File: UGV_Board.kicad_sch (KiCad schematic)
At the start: 19 parts, among them J1 I2C_EXPANSION, J2 Debug Header, J3 ESP_Header, SW1 SW_MCU_EN, SW2 SW_PICO_RST, SW3 SW_ESP_RST, U1 SC0915, U2 SPX1117M3-L-3-3

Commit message: mcu control circuitry
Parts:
- added C?: 1uF, symbol Device:C
- added J?: RFLCTL_Header, symbol Connector:Conn_01x04_Female
- added J?: RFLCTR_Header, symbol Connector:Conn_01x04_Female
- added R? (x4): 330, Resistor_SMD:R_1206_3216Metric_Pad1.30x1.75mm_HandSolder, symbol Device:R_Small_US
- added R? (x2): 10k, Resistor_SMD:R_1206_3216Metric_Pad1.30x1.75mm_HandSolder, symbol Device:R_Small_US
- added RV? (x2): R_Potentiometer, symbol Device:R_Potentiometer
- added U? (x3): LM393, symbol Comparator:LM393
- J1: symbol Connector:Conn_01x02_Female -> Connector:Conn_01x04_Female
- R1, R2, R3, R4, R5, R6: value 220 -> 330
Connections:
- net +3V3: now also J1.4 (Pin_4), J?.2 (Pin_2), J?.2 (Pin_2), J?.4 (Pin_4), J?.4 (Pin_4), R?.2, R?.2, RV?.1, RV?.1, U?.8 (V+)
- net GND: now also J1.1 (Pin_1), C?.2, R?.1, R?.1, R?.1, R?.1, RV?.3, RV?.3, U?.4 (V-)
- net SCL: now also J1.2 (Pin_2), R?.1; no longer J1.1 (Pin_1)
- net SDA: now also J1.3 (Pin_3), R?.1; no longer J1.2 (Pin_2)
- net at SW2.1, U1.30 (RUN): now also C?.1
- net ENCL_SIG: now reaches U1.19 (I2C1_SDA/SPI1_SCK/GP14)
- net ENCL_SIG: now also U?.7
- net ENCR_SIG: now reaches U1.20 (I2C1_SCL/SPI1_TX/GP15)
- net ENCR_SIG: now also U?.1
- new net: J?.3 (Pin_3), R?.2 (x2)
- new net: RV?.2, U?.6 (_)
- new net: RV?.2, U?.2 (-)
- new net: J?.1 (Pin_1), R?.2, U?.3 (+)
- new net: J?.1 (Pin_1), R?.2, U?.5 (+)
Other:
- note added: "*ESP-01 reset switch, 12k pullup & 1uF debounce internal"
- note added: "*Igor/Yusuf feel free to make a separate ground line if you're going for total isolation. Delete this text when you're done. Also feel free to wipe this regulator with your own 3.3V line"
- note added: "*MCU PWR/IO line voltage, regulated: 3.3V max current: 800mA"
- note added: "*PICO reset swtich, 50k pullup internal"
- note added: "12k internal pullup"
- note added: "1k -> Blue LED, active low"
- note added: "Reflective Sensor + Comparator Logic"
- note removed: "*ESP-01 reset switch"
- note removed: "*Igor/Yusuf feel free to make a separate ground line if you're going for total isolation. Delete this text when you're done."
- note removed: "*MCU PWR/IO line"
- note removed: "*PICO reset swtich"
- moved on the sheet: D1, D3, R1, R3, R5

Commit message: Buck + H-Bridge
Added
-Buck Convertor
-H-Bridge
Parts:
- added C1: 10uF, symbol Device:C_Small
- added C2: 22uF, symbol Device:C_Small
- added C2: 22 uF, symbol Device:C_Small
- added C3: 100nF, symbol Device:C_Small
- added J7, J8: Conn_01x02_Female, symbol Connector:Conn_01x02_Female
- added L1: 4.7uH, symbol Device:L
- added R2: 10k, Resistor_SMD:R_1206_3216Metric_Pad1.30x1.75mm_HandSolder, symbol Device:R_Small_US
- added RV3: R_Potentiometer, symbol Device:R_Potentiometer
- added U4: BD63565EFV-E2, BD63565EFV-E2_ROM, symbol H bridge:BD63565EFV-E2
- added U5: AP62200WU-7, TSOT26-WU_DIO, symbol Buck Convertor:AP62200WU-7
- R10, R7, R8, R9: renamed from R?; value 330 -> 220
- gave numbers to parts that had none: 9
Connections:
- net +3V3: now also U4.17 (PS), U4.20 (VCC), U5.5 (EN)
- net +7.5V: now also C1.1, U5.3 (VIN)
- net GND: now also C1.2, C2.2, C2.2, R2.1, U4.1 (GND), U4.13 (PGND), U4.4 (PWM), U4.8 (PGND), U5.1 (GND)
- new net: C3.1, L1.2, U5.2 (SW)
- new net: R2.2, RV3.2, U5.4 (FB)
- new net: C3.2, U5.6 (BST)
- new net: J7.1 (Pin_1), U4.6 (OUT1A), U4.7 (OUT1A)
- new net: J7.2 (Pin_2), U4.10 (OUT1B), U4.9 (OUT1B)
- new net: J8.2 (Pin_2), U4.11 (OUT2B), U4.12 (OUT2B)
- new net: J8.1 (Pin_1), U4.14 (OUT2A), U4.15 (OUT2A)
- new net +6V: C2.1, C2.1, L1.1, RV3.3, U4.16 (VM), U4.5 (VM)
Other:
- note added: "Buck Convertor"
- note added: "H-Bridge"
- note added: "Pico-Microcontroller"
- moved on the sheet: J3

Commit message: Assigned footprints
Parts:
- C1, C2, C3, C4: footprint (none) -> Capacitor_SMD:C_1206_3216Metric_Pad1.33x1.80mm_HandSolder
- C5: renamed from C2; footprint (none) -> Capacitor_SMD:C_1206_3216Metric_Pad1.33x1.80mm_HandSolder
- J4, J5: footprint (none) -> Connector_PinSocket_2.54mm:PinSocket_1x04_P2.54mm_Vertical
- J6: footprint (none) -> Connector_PinSocket_2.54mm:PinSocket_1x08_P2.54mm_Vertical
- J7, J8: footprint (none) -> Connector_PinSocket_2.54mm:PinSocket_1x02_P2.54mm_Vertical
- L1: footprint (none) -> Inductor_SMD:L_1210_3225Metric_Pad1.42x2.65mm_HandSolder
- RV1, RV2, RV3: footprint (none) -> Potentiometer_SMD:Potentiometer_Bourns_TC33X_Vertical
- U3: footprint (none) -> Package_DIP:DIP-8_W7.62mm_LongPads
- U4: footprint BD63565EFV-E2_ROM -> Drivers_3rdParty:BD63565EFV-E2
- U5: footprint TSOT26-WU_DIO -> SMPS_3rdParty:AP62200WU-7
- renumbered R2 to R13
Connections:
- net +3V3 renamed +3.3V

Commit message: floating en pin
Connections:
- net +3.3V: no longer U5.5 (EN)
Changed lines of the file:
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@@
     (pin "3")
-  )
-  (symbol (lib_name "+3.3V_10") (lib_id "power:+3.3V") (at 398.78 124.46 270) (unit 1)
-    (in_bom yes) (on_board yes) (fields_autoplaced)
-    (property "Reference" "#PWR0134" (id 0) (at 394.97 124.46 0)
-      (effects (font (size 1.27 1.27)) hide)
-    )
-    (property "Value" "+3.3V" (id 1) (at 402.59 124.4599 90)
-      (effects (font (size 1.27 1.27)) (justify left))
-    )
-    (property "Footprint" "" (id 2) (at 398.78 124.46 0)
-      (effects (font (size 1.27 1.27)) hide)
-    )
-    (property "Datasheet" "" (id 3) (at 398.78 124.46 0)
-      (effects (font (size 1.27 1.27)) hide)
-    )
-    (pin "1")
   )
   (symbol (lib_id "Device:R_Potentiometer") (at 341.63 137.16 270) (unit 1)
@@
       (reference "#PWR0133") (unit 1) (value "GND") (footprint "")
     )
-    (path "/76fdc603-9607-4e8b-ba75-955278b1b684"
-      (reference "#PWR0134") (unit 1) (value "+3.3V") (footprint "")
-    )
     (path "/8a73a5c8-b6b2-4b9f-a45b-d6aa4f2ccad5"

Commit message: fixed i2c header footprint
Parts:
- J1: footprint Connector_PinSocket_2.54mm:PinSocket_1x02_P2.54mm_Vertical -> Connector_PinSocket_2.54mm:PinSocket_1x04_P2.54mm_Vertical
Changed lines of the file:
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@@
     (property "Reference" "J1" (id 0) (at 276.86 267.97 0))
     (property "Value" "I2C_EXPANSION" (id 1) (at 276.86 270.51 0))
-    (property "Footprint" "Connector_PinSocket_2.54mm:PinSocket_1x02_P2.54mm_Vertical" (id 2) (at 279.4 278.13 0)
+    (property "Footprint" "Connector_PinSocket_2.54mm:PinSocket_1x04_P2.54mm_Vertical" (id 2) (at 279.4 278.13 0)
       (effects (font (size 1.27 1.27)) hide)
     )
@@
     )
     (path "/42fa0348-d6f3-440b-802f-dcef76e8d02c"
-      (reference "J1") (unit 1) (value "I2C_EXPANSION") (footprint "Connector_PinSocket_2.54mm:PinSocket_1x02_P2.54mm_Vertical")
+      (reference "J1") (unit 1) (value "I2C_EXPANSION") (footprint "Connector_PinSocket_2.54mm:PinSocket_1x04_P2.54mm_Vertical")
     )
     (path "/75c2a44c-2138-4e6a-93e2-ed701bb8f3d2"

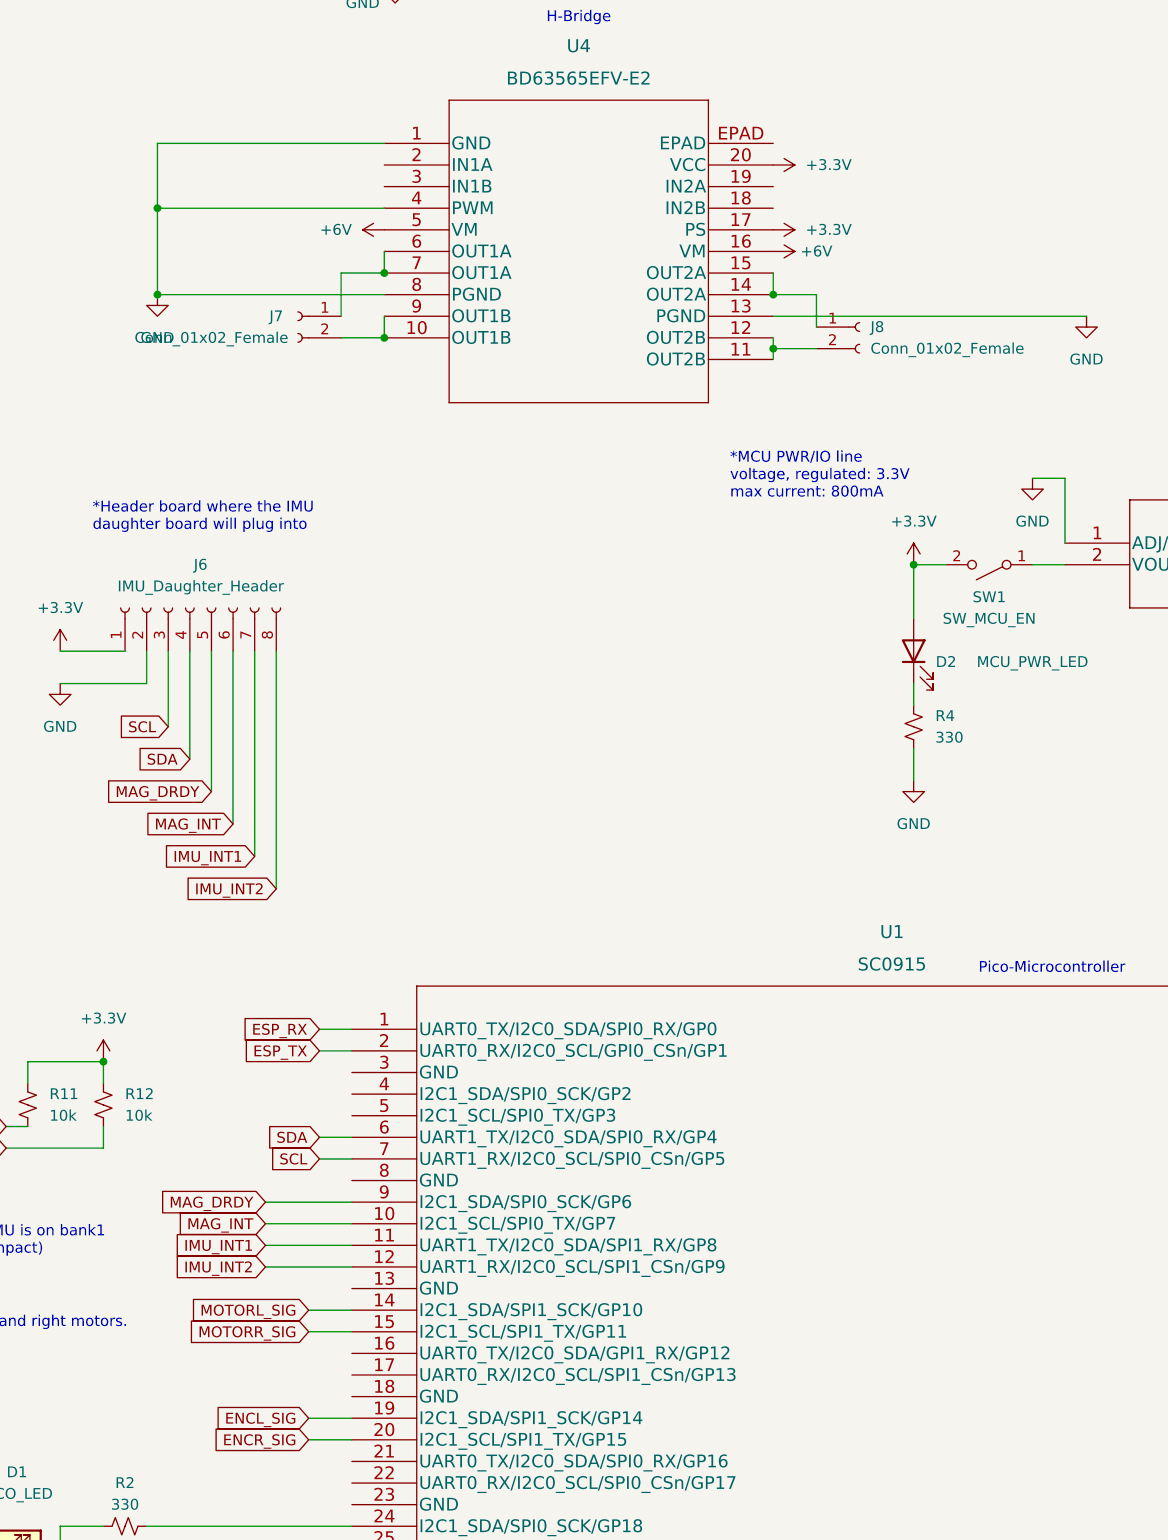
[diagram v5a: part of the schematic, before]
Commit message: plugged mcu into h-bridge
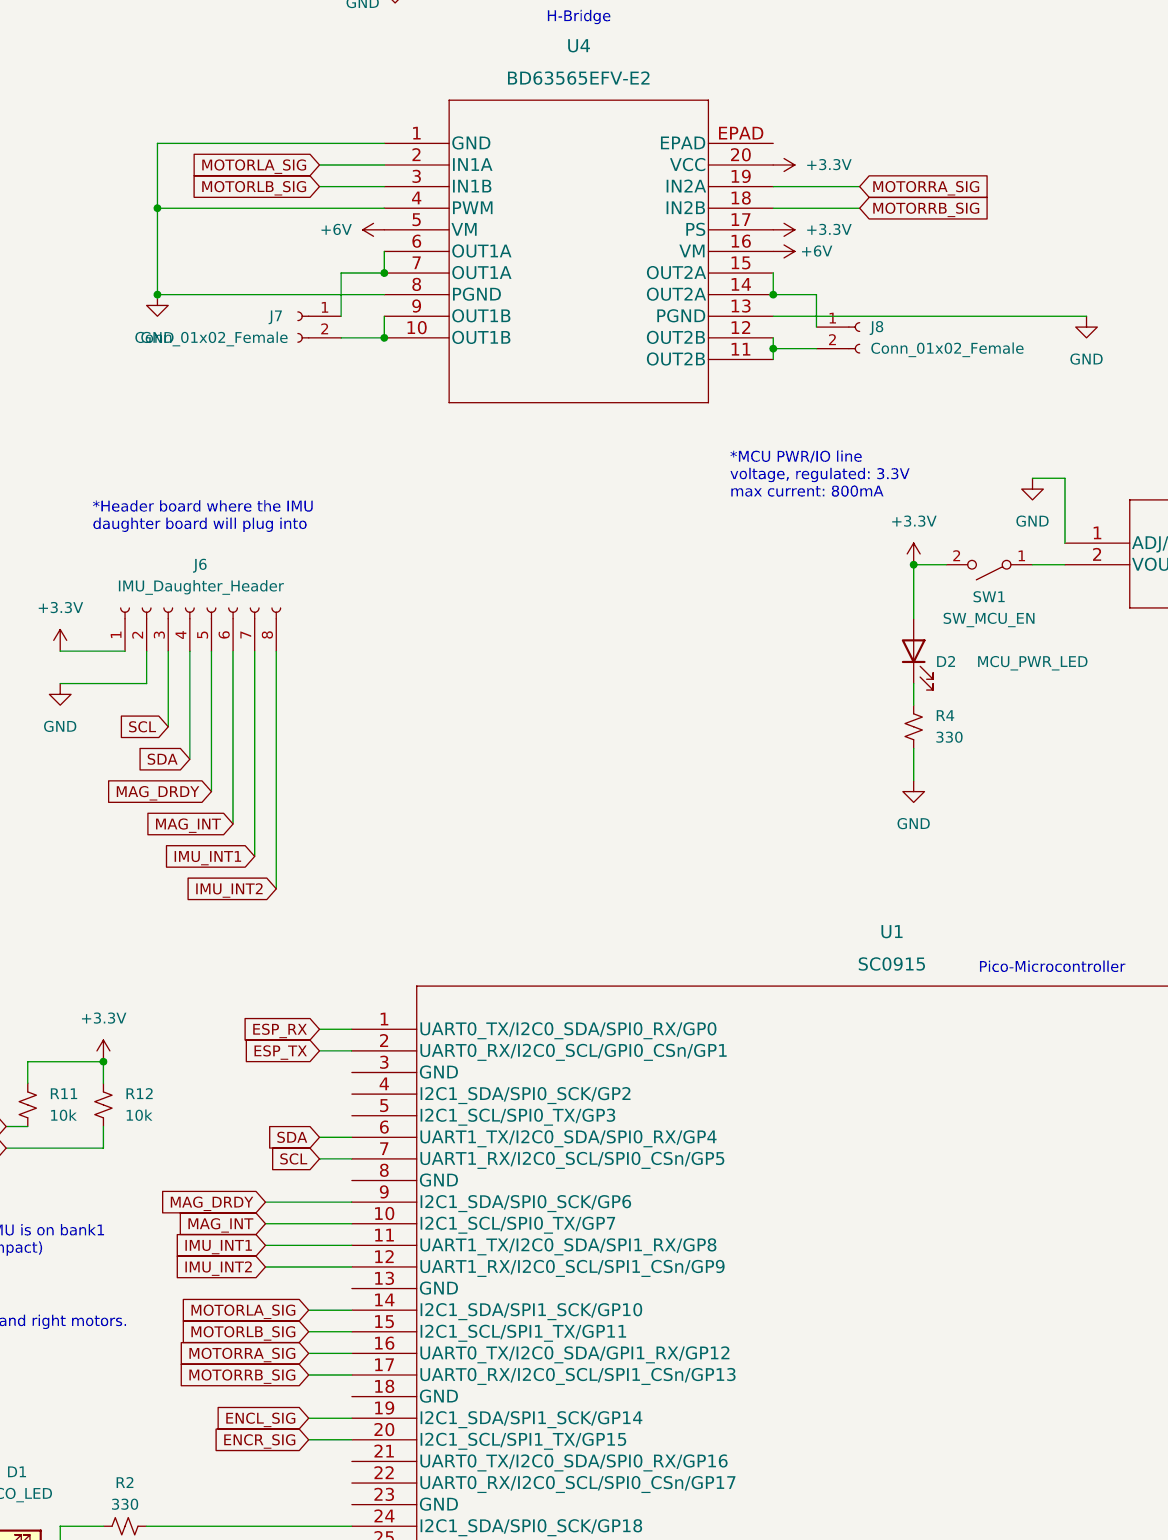
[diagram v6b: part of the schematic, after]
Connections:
- net MOTORL_SIG is gone; now on net MOTORLA_SIG: U1.14 (I2C1_SDA/SPI1_SCK/GP10)
- net MOTORR_SIG is gone; now on net MOTORLB_SIG: U1.15 (I2C1_SCL/SPI1_TX/GP11)
- net MOTORRB_SIG: now reaches U4.18 (IN2B)
- net MOTORRB_SIG: now also U1.17 (UART0_RX/I2C0_SCL/SPI1_CSn/GP13)
- net MOTORRA_SIG: now reaches U4.19 (IN2A)
- net MOTORRA_SIG: now also U1.16 (UART0_TX/I2C0_SDA/GPI1_RX/GP12)
- net MOTORLA_SIG: now reaches U4.2 (IN1A)
- net MOTORLB_SIG: now reaches U4.3 (IN1B)
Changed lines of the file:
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@@
+    (stroke (width 0) (type default) (color 0 0 0 0))
+  )
+  (wire (pts (xy 402.59 181.61) (xy 412.75 181.61))
     (stroke (width 0) (type default) (color 0 0 0 0))
   )
@@
     (stroke (width 0) (type default) (color 0 0 0 0))
   )
+  (wire (pts (xy 349.25 181.61) (xy 356.87 181.61))
+    (stroke (width 0) (type default) (color 0 0 0 0))
+  )
   (wire (pts (xy 177.8 365.76) (xy 223.52 365.76))
     (stroke (width 0) (type default) (color 0 0 0 0))
@@
     (stroke (width 0) (type default) (color 0 0 0 0))
   )
+  (wire (pts (xy 347.98 318.77) (xy 353.06 318.77))
+    (stroke (width 0) (type default) (color 0 0 0 0))
+  )
   (wire (pts (xy 284.48 278.13) (xy 289.56 278.13))
     (stroke (width 0) (type default) (color 0 0 0 0))
@@
     (stroke (width 0) (type default) (color 0 0 0 0))
   )
+  (wire (pts (xy 402.59 184.15) (xy 412.75 184.15))
+    (stroke (width 0) (type default) (color 0 0 0 0))
+  )
   (wire (pts (xy 224.79 287.02) (xy 224.79 289.56))
     (stroke (width 0) (type default) (color 0 0 0 0))
@@
     (stroke (width 0) (type default) (color 0 0 0 0))
   )
+  (wire (pts (xy 349.25 179.07) (xy 356.87 179.07))
+    (stroke (width 0) (type default) (color 0 0 0 0))
+  )
   (wire (pts (xy 557.53 259.08) (xy 560.07 259.08))
     (stroke (width 0) (type default) (color 0 0 0 0))
@@
   )
   (wire (pts (xy 187.96 360.68) (xy 187.96 367.03))
+    (stroke (width 0) (type default) (color 0 0 0 0))
+  )
+  (wire (pts (xy 347.98 321.31) (xy 353.06 321.31))
     (stroke (width 0) (type default) (color 0 0 0 0))
   )
@@
     )
   )
-  (global_label "MOTORR_SIG" (shape input) (at 347.98 316.23 180) (fields_autoplaced)
-    (effects (font (size 1.27 1.27)) (justify right))
-    (property "Intersheet References" "${INTERSHEET_REFS}" (id 0) (at 333.895 316.1506 0)
+  (global_label "MOTORLB_SIG" (shape input) (at 347.98 316.23 180) (fields_autoplaced)
+    (effects (font (size 1.27 1.27)) (justify right))
+    (property "Intersheet References" "${INTERSHEET_REFS}" (id 0) (at 332.8669 316.1506 0)
       (effects (font (size 1.27 1.27)) (justify right) hide)
     )
@@
     )
   )
+  (global_label "MOTORLA_SIG" (shape input) (at 349.25 179.07 180) (fields_autoplaced)
+    (effects (font (size 1.27 1.27)) (justify right))
+    (property "Intersheet References" "${INTERSHEET_REFS}" (id 0) (at 334.3183 178.9906 0)
+      (effects (font (size 1.27 1.27)) (justify right) hide)
+    )
+  )
   (global_label "ENCL_SIG" (shape input) (at 347.98 326.39 180) (fields_autoplaced)
     (effects (font (size 1.27 1.27)) (justify right))
@@
     )
   )
+  (global_label "MOTORLB_SIG" (shape input) (at 349.25 181.61 180) (fields_autoplaced)
+    (effects (font (size 1.27 1.27)) (justify right))
+    (property "Intersheet References" "${INTERSHEET_REFS}" (id 0) (at 334.1369 181.5306 0)
+      (effects (font (size 1.27 1.27)) (justify right) hide)
+    )
+  )
+  (global_label "MOTORRA_SIG" (shape input) (at 412.75 181.61 0) (fields_autoplaced)
+    (effects (font (size 1.27 1.27)) (justify left))
+    (property "Intersheet References" "${INTERSHEET_REFS}" (id 0) (at 427.9236 181.6894 0)
+      (effects (font (size 1.27 1.27)) (justify left) hide)
+    )
+  )
   (global_label "MAG_INT" (shape input) (at 339.09 256.54 180) (fields_autoplaced)
     (effects (font (size 1.27 1.27)) (justify right))
@@
     )
   )
+  (global_label "MOTORRB_SIG" (shape input) (at 347.98 321.31 180) (fields_autoplaced)
+    (effects (font (size 1.27 1.27)) (justify right))
+    (property "Intersheet References" "${INTERSHEET_REFS}" (id 0) (at 332.625 321.2306 0)
+      (effects (font (size 1.27 1.27)) (justify right) hide)
+    )
+  )
   (global_label "ESP_RX" (shape input) (at 542.29 251.46 180) (fields_autoplaced)
     (effects (font (size 1.27 1.27)) (justify right))
@@
     )
   )
+  (global_label "MOTORRB_SIG" (shape input) (at 412.75 184.15 0) (fields_autoplaced)
+    (effects (font (size 1.27 1.27)) (justify left))
+    (property "Intersheet References" "${INTERSHEET_REFS}" (id 0) (at 428.105 184.2294 0)
+      (effects (font (size 1.27 1.27)) (justify left) hide)
+    )
+  )
   (global_label "SDA" (shape input) (at 312.42 292.1 180) (fields_autoplaced)
     (effects (font (size 1.27 1.27)) (justify right))
@@
     )
   )
+  (global_label "MOTORRA_SIG" (shape input) (at 347.98 318.77 180) (fields_autoplaced)
+    (effects (font (size 1.27 1.27)) (justify right))
+    (property "Intersheet References" "${INTERSHEET_REFS}" (id 0) (at 332.8064 318.6906 0)
+      (effects (font (size 1.27 1.27)) (justify right) hide)
+    )
+  )
   (global_label "MAG_DRDY" (shape input) (at 336.55 252.73 180) (fields_autoplaced)
     (effects (font (size 1.27 1.27)) (justify right))
@@
     )
   )
-  (global_label "MOTORL_SIG" (shape input) (at 347.98 313.69 180) (fields_autoplaced)
-    (effects (font (size 1.27 1.27)) (justify right))
-    (property "Intersheet References" "${INTERSHEET_REFS}" (id 0) (at 334.1369 313.6106 0)
-      (effects (font (size 1.27 1.27)) (justify right) hide)
-    )
+  (global_label "MOTORLA_SIG" (shape input) (at 347.98 313.69 180) (fields_autoplaced)
+    (effects (font (size 1.27 1.27)) (justify right))
+    (property "Intersheet References" "${INTERSHEET_REFS}" (id 0) (at 333.0483 313.6106 0)
+      (effects (font (size 1.27 1.27)) (justify right) hide)
+    )
